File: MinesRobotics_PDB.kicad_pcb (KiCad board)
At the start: 2 copper layers, 101.1 x 75.9 mm, 57 parts, among them J1 Conn_01x02_Female, J2 Conn_01x02_Female, J3 Conn_01x02_Female, J4 Conn_01x02_Female, J5 Conn_01x02_Female, J6 Conn_01x02_Female, J7 Conn_01x02_Female, J8 Conn_01x02_Female, J9 Conn_01x02_Female, U1 I6A4W020A033V-003-R

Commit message: Did some initial board layout
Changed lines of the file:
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@@
       (sketchpadsonfab false)
       (subtractmaskfromsilk false)
-      (outputformat 4)
+      (outputformat 1)
       (mirror false)
       (drillshape 0)
       (scaleselection 1)
-      (outputdirectory "Production/Drawings/PCBDrawings/")
+      (outputdirectory "Production/Gerbers/")
     )
   )
@@
     (fp_line (start -1 0.625) (end -1 -0.625) (layer "F.Fab") (width 0.1))
     (fp_line (start 1 0.625) (end -1 0.625) (layer "F.Fab") (width 0.1))
-    (pad "1" smd roundrect (at -0.9125 0) (size 1.025 1.4) (layers "F.Cu" "F.Paste" "F.Mask") (roundrect_rratio 0.243902)
+    (pad "1" smd roundrect (at -0.9125 0) (size 1.025 1.4) (layers "F.Cu" "F.Paste" "F.Mask") (roundrect_rratio 0.243902439)
       (net 21 "Net-(D3-Pad1)") (pintype "passive"))
-    (pad "2" smd roundrect (at 0.9125 0) (size 1.025 1.4) (layers "F.Cu" "F.Paste" "F.Mask") (roundrect_rratio 0.243902)
+    (pad "2" smd roundrect (at 0.9125 0) (size 1.025 1.4) (layers "F.Cu" "F.Paste" "F.Mask") (roundrect_rratio 0.243902439)
       (net 9 "/Fuses/GATE_LIFT_MOTOR_1") (pintype "passive"))
     (model "${KICAD6_3DMODEL_DIR}/Resistor_SMD.3dshapes/R_0805_2012Metric.wrl"
@@
     (fp_line (start -1 -0.625) (end 1 -0.625) (layer "F.Fab") (width 0.1))
     (fp_line (start 1 0.625) (end -1 0.625) (layer "F.Fab") (width 0.1))
-    (pad "1" smd roundrect (at -0.9125 0 270) (size 1.025 1.4) (layers "F.Cu" "F.Paste" "F.Mask") (roundrect_rratio 0.243902)
+    (pad "1" smd roundrect (at -0.9125 0 270) (size 1.025 1.4) (layers "F.Cu" "F.Paste" "F.Mask") (roundrect_rratio 0.243902439)
       (net 24 "Net-(D6-Pad1)") (pintype "passive"))
-    (pad "2" smd roundrect (at 0.9125 0 270) (size 1.025 1.4) (layers "F.Cu" "F.Paste" "F.Mask") (roundrect_rratio 0.243902)
+    (pad "2" smd roundrect (at 0.9125 0 270) (size 1.025 1.4) (layers "F.Cu" "F.Paste" "F.Mask") (roundrect_rratio 0.243902439)
       (net 6 "/Fuses/DRIVE_MOTOR_RIGHT_REAR") (pintype "passive"))
     (model "${KICAD6_3DMODEL_DIR}/Resistor_SMD.3dshapes/R_0805_2012Metric.wrl"
@@
     (fp_line (start -1 0.625) (end -1 -0.625) (layer "F.Fab") (width 0.1))
     (fp_line (start -1 -0.625) (end 1 -0.625) (layer "F.Fab") (width 0.1))
-    (pad "1" smd roundrect (at -0.9125 0) (size 1.025 1.4) (layers "F.Cu" "F.Paste" "F.Mask") (roundrect_rratio 0.243902)
-      (net 1 "+24V") (pintype "passive"))
-    (pad "2" smd roundrect (at 0.9125 0) (size 1.025 1.4) (layers "F.Cu" "F.Paste" "F.Mask") (roundrect_rratio 0.243902)
+    (pad "1" smd roundrect (at -0.9125 0) (size 1.025 1.4) (layers "F.Cu" "F.Paste" "F.Mask") (roundrect_rratio 0.243902439)
+      (net 1 "+24V") (pintype "passive"))
+    (pad "2" smd roundrect (at 0.9125 0) (size 1.025 1.4) (layers "F.Cu" "F.Paste" "F.Mask") (roundrect_rratio 0.243902439)
       (net 12 "Net-(R1-Pad2)") (pintype "passive"))
     (model "${KICAD6_3DMODEL_DIR}/Resistor_SMD.3dshapes/R_0805_2012Metric.wrl"
@@
     (fp_line (start -1 0.625) (end -1 -0.625) (layer "F.Fab") (width 0.1))
     (fp_line (start 1 0.625) (end -1 0.625) (layer "F.Fab") (width 0.1))
-    (pad "1" smd roundrect (at -0.9125 0 90) (size 1.025 1.4) (layers "F.Cu" "F.Paste" "F.Mask") (roundrect_rratio 0.243902)
+    (pad "1" smd roundrect (at -0.9125 0 90) (size 1.025 1.4) (layers "F.Cu" "F.Paste" "F.Mask") (roundrect_rratio 0.243902439)
       (net 19 "Net-(D1-Pad1)") (pintype "passive"))
-    (pad "2" smd roundrect (at 0.9125 0 90) (size 1.025 1.4) (layers "F.Cu" "F.Paste" "F.Mask") (roundrect_rratio 0.243902)
+    (pad "2" smd roundrect (at 0.9125 0 90) (size 1.025 1.4) (layers "F.Cu" "F.Paste" "F.Mask") (roundrect_rratio 0.243902439)
       (net 3 "/Fuses/DRIVE_MOTOR_LEFT_FRONT") (pintype "passive"))
     (model "${KICAD6_3DMODEL_DIR}/Resistor_SMD.3dshapes/R_0805_2012Metric.wrl"
@@
     (fp_line (start 1 0.625) (end -1 0.625) (layer "F.Fab") (width 0.1))
     (fp_line (start 1 -0.625) (end 1 0.625) (layer "F.Fab") (width 0.1))
-    (pad "1" smd roundrect (at -0.9125 0 180) (size 1.025 1.4) (layers "F.Cu" "F.Paste" "F.Mask") (roundrect_rratio 0.243902)
+    (pad "1" smd roundrect (at -0.9125 0 180) (size 1.025 1.4) (layers "F.Cu" "F.Paste" "F.Mask") (roundrect_rratio 0.243902439)
       (net 25 "Net-(D7-Pad1)") (pintype "passive"))
-    (pad "2" smd roundrect (at 0.9125 0 180) (size 1.025 1.4) (layers "F.Cu" "F.Paste" "F.Mask") (roundrect_rratio 0.243902)
+    (pad "2" smd roundrect (at 0.9125 0 180) (size 1.025 1.4) (layers "F.Cu" "F.Paste" "F.Mask") (roundrect_rratio 0.243902439)
       (net 10 "/Fuses/GATE_LIFT_MOTOR_2") (pintype "passive"))
     (model "${KICAD6_3DMODEL_DIR}/Resistor_SMD.3dshapes/R_0805_2012Metric.wrl"
@@
     (fp_line (start -1 -0.625) (end 1 -0.625) (layer "F.Fab") (width 0.1))
     (fp_line (start -1 0.625) (end -1 -0.625) (layer "F.Fab") (width 0.1))
-    (pad "1" smd roundrect (at -0.9125 0 270) (size 1.025 1.4) (layers "F.Cu" "F.Paste" "F.Mask") (roundrect_rratio 0.243902)
+    (pad "1" smd roundrect (at -0.9125 0 270) (size 1.025 1.4) (layers "F.Cu" "F.Paste" "F.Mask") (roundrect_rratio 0.243902439)
       (net 26 "Net-(D8-Pad1)") (pintype "passive"))
-    (pad "2" smd roundrect (at 0.9125 0 270) (size 1.025 1.4) (layers "F.Cu" "F.Paste" "F.Mask") (roundrect_rratio 0.243902)
+    (pad "2" smd roundrect (at 0.9125 0 270) (size 1.025 1.4) (layers "F.Cu" "F.Paste" "F.Mask") (roundrect_rratio 0.243902439)
       (net 8 "/Fuses/PLUNGE_MOTOR") (pintype "passive"))
     (model "${KICAD6_3DMODEL_DIR}/Resistor_SMD.3dshapes/R_0805_2012Metric.wrl"
@@
     (fp_line (start 1 0.625) (end -1 0.625) (layer "F.Fab") (width 0.1))
     (fp_line (start -1 -0.625) (end 1 -0.625) (layer "F.Fab") (width 0.1))
-    (pad "1" smd roundrect (at -0.9125 0) (size 1.025 1.4) (layers "F.Cu" "F.Paste" "F.Mask") (roundrect_rratio 0.243902)
+    (pad "1" smd roundrect (at -0.9125 0) (size 1.025 1.4) (layers "F.Cu" "F.Paste" "F.Mask") (roundrect_rratio 0.243902439)
       (net 13 "Net-(R2-Pad1)") (pintype "passive"))
-    (pad "2" smd roundrect (at 0.9125 0) (size 1.025 1.4) (layers "F.Cu" "F.Paste" "F.Mask") (roundrect_rratio 0.243902)
+    (pad "2" smd roundrect (at 0.9125 0) (size 1.025 1.4) (layers "F.Cu" "F.Paste" "F.Mask") (roundrect_rratio 0.243902439)
       (net 14 "Net-(R2-Pad2)") (pintype "passive"))
     (model "${KICAD6_3DMODEL_DIR}/Resistor_SMD.3dshapes/R_0805_2012Metric.wrl"
@@
     (fp_line (start 1 -0.625) (end 1 0.625) (layer "F.Fab") (width 0.1))
     (fp_line (start -1 -0.625) (end 1 -0.625) (layer "F.Fab") (width 0.1))
-    (pad "1" smd roundrect (at -0.9125 0 90) (size 1.025 1.4) (layers "F.Cu" "F.Paste" "F.Mask") (roundrect_rratio 0.243902)
+    (pad "1" smd roundrect (at -0.9125 0 90) (size 1.025 1.4) (layers "F.Cu" "F.Paste" "F.Mask") (roundrect_rratio 0.243902439)
       (net 20 "Net-(D2-Pad1)") (pintype "passive"))
-    (pad "2" smd roundrect (at 0.9125 0 90) (size 1.025 1.4) (layers "F.Cu" "F.Paste" "F.Mask") (roundrect_rratio 0.243902)
+    (pad "2" smd roundrect (at 0.9125 0 90) (size 1.025 1.4) (layers "F.Cu" "F.Paste" "F.Mask") (roundrect_rratio 0.243902439)
       (net 5 "/Fuses/DRIVE_MOTOR_RIGHT_FRONT") (pintype "passive"))
     (model "${KICAD6_3DMODEL_DIR}/Resistor_SMD.3dshapes/R_0805_2012Metric.wrl"
@@
     (fp_line (start 1 -0.625) (end 1 0.625) (layer "F.Fab") (width 0.1))
     (fp_line (start -1 -0.625) (end 1 -0.625) (layer "F.Fab") (width 0.1))
-    (pad "1" smd roundrect (at -0.9125 0 270) (size 1.025 1.4) (layers "F.Cu" "F.Paste" "F.Mask") (roundrect_rratio 0.243902)
+    (pad "1" smd roundrect (at -0.9125 0 270) (size 1.025 1.4) (layers "F.Cu" "F.Paste" "F.Mask") (roundrect_rratio 0.243902439)
       (net 23 "Net-(D5-Pad1)") (pintype "passive"))
-    (pad "2" smd roundrect (at 0.9125 0 270) (size 1.025 1.4) (layers "F.Cu" "F.Paste" "F.Mask") (roundrect_rratio 0.243902)
+    (pad "2" smd roundrect (at 0.9125 0 270) (size 1.025 1.4) (layers "F.Cu" "F.Paste" "F.Mask") (roundrect_rratio 0.243902439)
       (net 4 "/Fuses/DRIVE_MOTOR_LEFT_REAR") (pintype "passive"))
     (model "${KICAD6_3DMODEL_DIR}/Resistor_SMD.3dshapes/R_0805_2012Metric.wrl"
@@
     (fp_line (start 1 0.625) (end -1 0.625) (layer "F.Fab") (width 0.1))
     (fp_line (start 1 -0.625) (end 1 0.625) (layer "F.Fab") (width 0.1))
-    (pad "1" smd roundrect (at -0.9125 0 270) (size 1.025 1.4) (layers "F.Cu" "F.Paste" "F.Mask") (roundrect_rratio 0.243902)
+    (pad "1" smd roundrect (at -0.9125 0 270) (size 1.025 1.4) (layers "F.Cu" "F.Paste" "F.Mask") (roundrect_rratio 0.243902439)
       (net 22 "Net-(D4-Pad1)") (pintype "passive"))
-    (pad "2" smd roundrect (at 0.9125 0 270) (size 1.025 1.4) (layers "F.Cu" "F.Paste" "F.Mask") (roundrect_rratio 0.243902)
+    (pad "2" smd roundrect (at 0.9125 0 270) (size 1.025 1.4) (layers "F.Cu" "F.Paste" "F.Mask") (roundrect_rratio 0.243902439)
       (net 7 "/Fuses/DIG_MOTOR") (pintype "passive"))
     (model "${KICAD6_3DMODEL_DIR}/Resistor_SMD.3dshapes/R_0805_2012Metric.wrl"

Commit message: Trying things
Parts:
- moved J1 7.43 mm to (122.7, 80.0), turned to -90 degrees
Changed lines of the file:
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@@
       (sketchpadsonfab false)
       (subtractmaskfromsilk false)
-      (outputformat 1)
+      (outputformat 4)
       (mirror false)
       (drillshape 0)
       (scaleselection 1)
-      (outputdirectory "Production/Gerbers/")
+      (outputdirectory "Production/Drawings/PCBDrawings/")
     )
   )
@@
   )
   (footprint "Connector_JST:JST_XH_B2B-XH-A_1x02_P2.50mm_Vertical" (layer "F.Cu")
-    (at 130 81.28)
+    (at 122.682 80.01 -90)
     (descr "JST XH series connector, B2B-XH-A (http://www.jst-mfg.com/product/pdf/eng/eXH.pdf), generated with kicad-footprint-generator")
     (tags "connector JST XH vertical")
@@
     (property "Sheetname" "Buck converter")
     (attr through_hole)
-    (fp_text reference "J1" (at 6.525 1.905) (layer "F.SilkS")
-      (effects (font (size 1 1) (thickness 0.15)))
-    )
-    (fp_text value "Conn_01x02_Female" (at 1.25 4.6) (layer "F.Fab") hide
-      (effects (font (size 1 1) (thickness 0.15)))
-    )
-    (fp_text user "${REFERENCE}" (at 1.25 2.7) (layer "F.Fab")
+    (fp_text reference "J1" (at 6.525 1.905 90) (layer "F.SilkS")
+      (effects (font (size 1 1) (thickness 0.15)))
+    )
+    (fp_text value "Conn_01x02_Female" (at 1.25 4.6 90) (layer "F.Fab") hide
+      (effects (font (size 1 1) (thickness 0.15)))
+    )
+    (fp_text user "${REFERENCE}" (at 1.25 2.7 90) (layer "F.Fab")
       (effects (font (size 1 1) (thickness 0.15)))
     )
@@
     (fp_line (start -0.625 -2.35) (end 0 -1.35) (layer "F.Fab") (width 0.1))
     (fp_line (start 0 -1.35) (end 0.625 -2.35) (layer "F.Fab") (width 0.1))
-    (pad "1" thru_hole roundrect (at 0 0) (size 1.7 2) (drill 1) (layers *.Cu *.Mask) (roundrect_rratio 0.1470588235)
+    (pad "1" thru_hole roundrect (at 0 0 270) (size 1.7 2) (drill 1) (layers *.Cu *.Mask) (roundrect_rratio 0.1470588235)
       (net 11 "+9V") (pinfunction "Pin_1") (pintype "passive"))
-    (pad "2" thru_hole oval (at 2.5 0) (size 1.7 2) (drill 1) (layers *.Cu *.Mask)
+    (pad "2" thru_hole oval (at 2.5 0 270) (size 1.7 2) (drill 1) (layers *.Cu *.Mask)
       (net 2 "GND") (pinfunction "Pin_2") (pintype "passive"))
     (model "${KICAD6_3DMODEL_DIR}/Connector_JST.3dshapes/JST_XH_B2B-XH-A_1x02_P2.50mm_Vertical.wrl"
@@
         (xy 152.146 95.25)
         (xy 124.46 95.25)
-        (xy 124.46 86.995)
-        (xy 124.46 78.232)
+        (xy 124.46 86.868)
+        (xy 121.158 86.868)
+        (xy 121.158 78.232)
         (xy 152.146 78.232)
       )

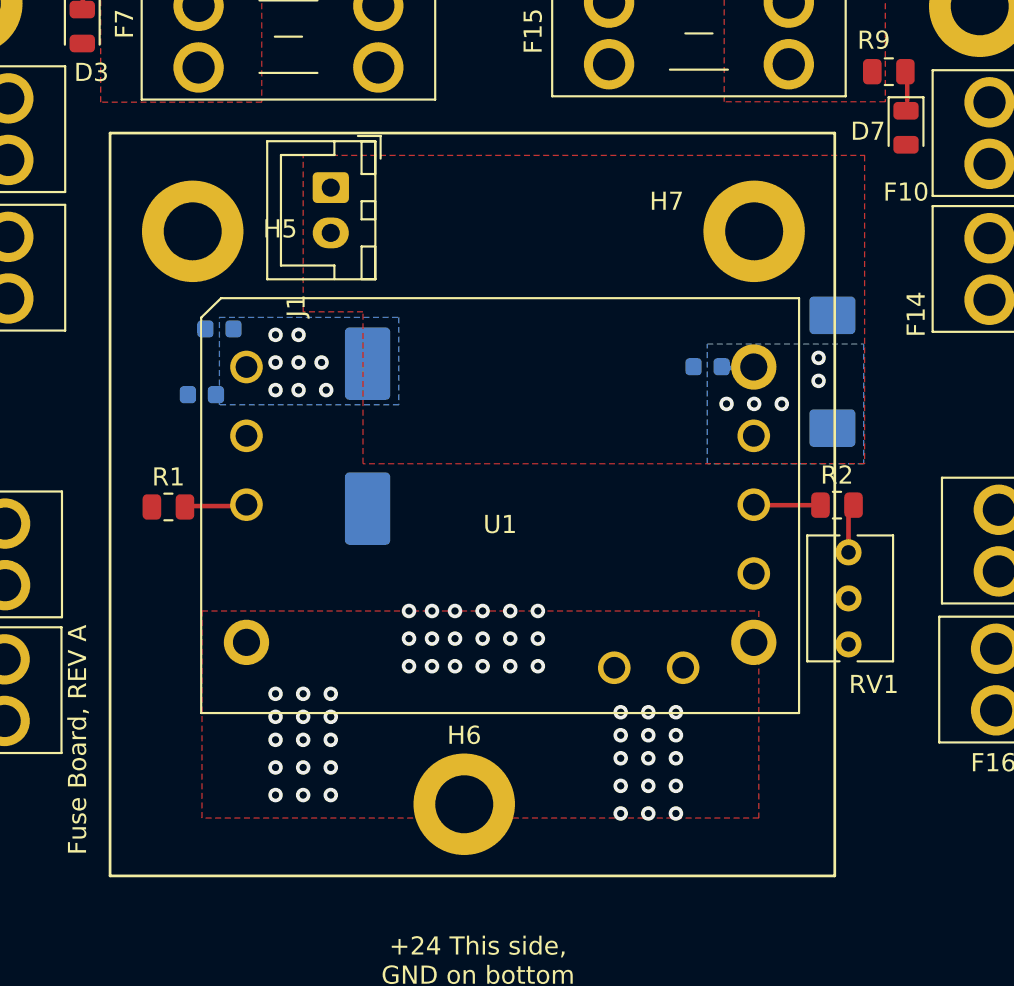
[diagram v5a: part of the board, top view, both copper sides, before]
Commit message: Moved daughter board up a tiny bit
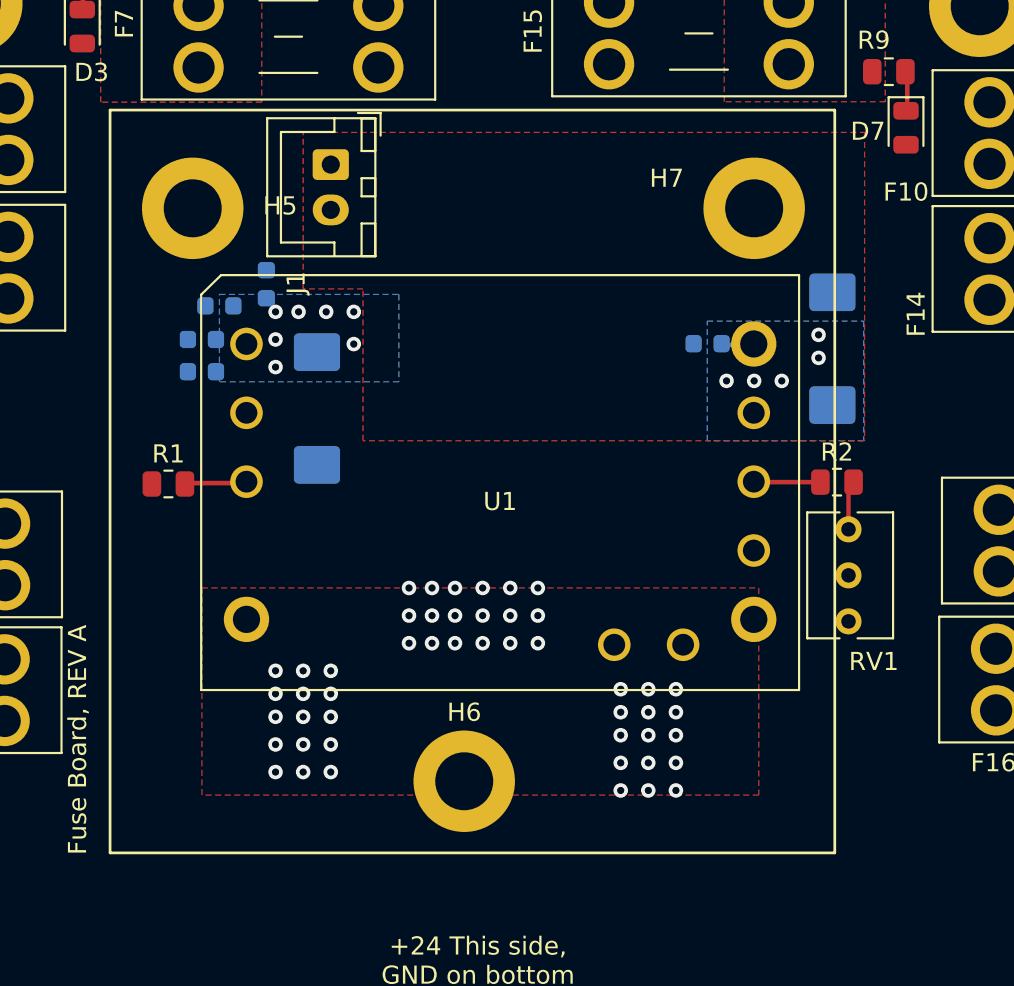
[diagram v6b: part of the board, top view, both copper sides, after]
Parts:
- added C4: 1u, Capacitor_SMD:C_0603_1608Metric, B.Cu at (115.6, 88.4)
- added C5: 22u, Capacitor_Tantalum_SMD:CP_EIA-7343-15_Kemet-W, B.Cu at (121.9, 92.2)
- C1: value 100u -> 10u; footprint Capacitor_SMD:CP_Elec_10x10 -> Capacitor_SMD:C_0603_1608Metric
- moved C1 10.1 mm to (119.1, 85.3), turned to 90 degrees
- moved H6 1.27 mm to (130.0, 112.8)
- moved J1 1.27 mm to (122.7, 78.7)
- moved RV1 1.27 mm to (151.3, 98.9)
- moved C2 1.27 mm to (143.5, 88.6)
- moved C3 1.27 mm to (150.4, 88.9)
- moved C7 1.27 mm to (116.5, 86.5)
- moved C8 1.27 mm to (115.6, 90.2)
- moved H5 1.27 mm to (115.1, 81.2)
- moved H7 1.27 mm to (146.1, 81.2)
- moved R1 1.27 mm to (113.7, 96.4)
- moved R2 1.27 mm to (150.6, 96.3)
- moved U1 1.27 mm to (132.0, 97.8)
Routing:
- net +24V: vias 8 -> 7

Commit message: fixed 9V regulator circuit
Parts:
- added D9: BZX8450-C2V2VL, Package_TO_SOT_SMD:SOT-23, F.Cu at (110.8, 92.4)
- added R11: 150, Resistor_SMD:R_0805_2012Metric, F.Cu at (113.9, 95.4)
- added R12: 10k, Resistor_SMD:R_0805_2012Metric, F.Cu at (114.9, 92.6)
- R1: value 100 -> 1k
- moved R1 7.22 mm to (113.8, 89.2), turned to -90 degrees
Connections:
- U1 pad 2: Net-(R1-Pad2) -> unconnected-(U1-Pad2)
- U1 pad 33: unconnected-(U1-Pad33) -> +24V
- U1 pad 34: unconnected-(U1-Pad34) -> Net-(U1-Pad34)
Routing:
- net +24V: track 0.00 -> 4.56 mm
- net Net-(R1-Pad2): track 3.53 -> 6.81 mm
- net GND: track 0.00 -> 3.12 mm, vias 48 -> 50
- net Net-(U1-Pad34): track 0.00 -> 2.31 mm

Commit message: Commiting before order, Regenerated gerbers for both boards
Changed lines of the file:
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@@
     (fp_line (start -0.625 -2.35) (end 0 -1.35) (layer "F.Fab") (width 0.1))
     (fp_line (start 0 -1.35) (end 0.625 -2.35) (layer "F.Fab") (width 0.1))
-    (pad "1" thru_hole roundrect (at 0 0 270) (size 1.7 2) (drill 1) (layers *.Cu *.Mask) (roundrect_rratio 0.1470588235)
+    (pad "1" thru_hole roundrect (at 0 0 270) (size 1.7 2) (drill 1.5) (layers *.Cu *.Mask) (roundrect_rratio 0.1470588235)
       (net 11 "+9V") (pinfunction "Pin_1") (pintype "passive"))
-    (pad "2" thru_hole oval (at 2.5 0 270) (size 1.7 2) (drill 1) (layers *.Cu *.Mask)
+    (pad "2" thru_hole oval (at 2.5 0 270) (size 1.7 2) (drill 1.5) (layers *.Cu *.Mask)
       (net 2 "GND") (pinfunction "Pin_2") (pintype "passive"))
     (model "${KICAD6_3DMODEL_DIR}/Connector_JST.3dshapes/JST_XH_B2B-XH-A_1x02_P2.50mm_Vertical.wrl"
